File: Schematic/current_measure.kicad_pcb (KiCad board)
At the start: 2 copper layers, 55 x 30.5 mm, 56 parts, among them J1 Conn_01x04_Pin, J2 Conn_01x02, J3 Screw_Terminal_01x02, J4 PowerSupply select, J5 Conn_02x03_Counter_Clockwise, J6 Conn_01x04, Q1 Si2319CDS, SW1 SW_Push, U1 MIC5365-3.3YD5, U2 INA186, U3 ISO652, U4 MCP6002-xSN, U5 OPA350, U6 STM32G431C8Tx, Y1 8MHz

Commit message: PCB small
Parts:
- removed the C11 at (179.4, 78.4)
- removed C22: 1µ, Capacitor_SMD:C_0805_2012Metric
- removed C23: 0.1µ, Capacitor_SMD:C_0805_2012Metric
- removed the C3 at (213.5, 63.5)
- removed J4: PowerSupply select, Connector_PinSocket_2.54mm:PinSocket_1x03_P2.54mm_Vertical
- added C20: 100n, Capacitor_SMD:C_0805_2012Metric, F.Cu at (103.0, 38.5)
- added JP1: SolderJumper_3_Open, Jumper:SolderJumper-3_P1.3mm_Open_Pad1.0x1.5mm, F.Cu at (77.8, 46.8)
- added U7: OPA333xxDBV, Package_TO_SOT_SMD:SOT-23-5_HandSoldering, F.Cu at (106.8, 39.0)
- RV1, RV2: footprint Potentiometer_THT:Potentiometer_Vishay_T73YP_Vertical -> Potentiometer_THT:Potentiometer_Bourns_3296Z_Horizontal
- U4: value MCP6002-xSN -> OPA333xxDBV; footprint Package_SO:SOIC-8_3.9x4.9mm_P1.27mm -> Package_TO_SOT_SMD:SOT-23-5
- Y1: footprint Crystal:Resonator_SMD-3Pin_7.2x3.0mm -> Crystal:Resonator_SMD_Murata_CSTxExxV-3Pin_3.0x1.1mm
- moved J2 180.9 mm to (83.0, 52.5), turned to 90 degrees
- moved D1 180.1 mm to (82.2, 48.2), turned to -90 degrees
- moved D2 171.4 mm to (77.8, 41.8), turned to -90 degrees
- moved U1 170.2 mm to (85.5, 40.8), turned to 90 degrees
- moved J3 143.8 mm to (79.8, 30.8), turned to -90 degrees
- moved R7 140.7 mm to (96.0, 44.8), turned to 180 degrees
- moved R5 139.3 mm to (95.8, 37.0), turned to 180 degrees
- moved J1 139.2 mm to (127.4, 27.4), turned to -90 degrees
- moved R2 138.4 mm to (84.6, 32.0), turned to -90 degrees
- moved U5 137.0 mm to (95.8, 41.0), turned to 180 degrees
- moved U3 136.6 mm to (121.5, 33.5)
- moved R3 135.9 mm to (87.6, 33.0), turned to 0 degrees
- moved D4 135.7 mm to (128.5, 40.7), turned to -90 degrees
- moved D3 134.3 mm to (128.2, 48.0), turned to 90 degrees
- moved R6 133.8 mm to (94.0, 35.0), turned to 0 degrees
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- renumbered C12 to C10, C13 to C11, C14 to C12, C15 to C13, C16 to C14, C17 to C15, C18 to C16, C19 to C17, C20 to C18, C21 to C19, C4 to C3, C5 to C4, C6 to C5, C7 to C6, C8 to C7, C9 to C8, C10 to C9
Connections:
- net /xTAL_{1} renamed /xTAL+
- net /xTAL_{2} renamed /xTAL-
- J5 pad 6: Net-(J4-Pin_2) -> /V_{prog}
- J6 pad 1: GND -> MCU_I2C_SDA
- J6 pad 3: MCU_I2C_SDA -> +3.3V
- J6 pad 4: +3.3V -> GND
- R4 pad 2: Net-(U4A-+) -> Net-(U4-+)
- R5 pad 1: Net-(U5-+) -> Net-(U5--)
- R6 pad 2: Net-(U5-+) -> Net-(U5--)
- R8 pad 2: Net-(U5--) -> Net-(U5-+)
- R9 pad 1: Net-(U5--) -> Net-(U5-+)
- RV1 pad 1: Net-(U4A-+) -> GND
- RV1 pad 2: GND -> Net-(U4-+)
- RV1 pad 3: GND -> Net-(U4-+)
- RV2 pad 1: Net-(U5--) -> Net-(U5-+)
- U4 pad 2: REF_{offset} -> +3.3V
- U4 pad 3: Net-(U4A-+) -> Net-(U4-+)
- U4 pad 4: GND -> REF_{offset}
- U4 pad 5: V_{ref} -> GND
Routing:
- net /V_{prog}: track 0.00 -> 48.0 mm, vias 0 -> 6
- net GND: track 1.50 -> 34.0 mm, vias 7 -> 45
- net +5V: track 0.00 -> 29.1 mm, vias 0 -> 2
- net +3.3V: track 0.00 -> 27.2 mm, vias 0 -> 37
- net /~{RESET}: track 0.00 -> 23.9 mm, vias 0 -> 2
- net +3.3VP: track 0.00 -> 21.7 mm, vias 0 -> 2
- net Net-(U4-+): track 0.00 -> 20.4 mm
- net GPIO_LED: track 0.00 -> 19.7 mm, vias 0 -> 2
- net MCU_I2C_SCL: track 0.00 -> 18.9 mm, vias 0 -> 1
- net V_{buf}: track 0.00 -> 16.3 mm
- net MCU_RxD: track 0.00 -> 15.8 mm
- net MCU_I2C_SDA: track 0.00 -> 15.6 mm, vias 0 -> 1
- net ADC_in: track 0.00 -> 15.1 mm
- net MCU_TxD: track 0.00 -> 14.6 mm
- net Net-(U5-+): track 0.00 -> 14.5 mm, vias 0 -> 1
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- added copper zone on In2.Cu, net +3.3V
- added copper zone on B.Cu, net /V_{prog}
- added copper zone on F.Cu, net /V_{prog}
- added copper zone on In1.Cu, net GND
- removed copper zone on F.Cu, net USB_+5
- removed copper zone on F.Cu, net USB_GND
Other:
- board size 55 x 30.5 mm -> 55 x 30 mm
- copper layers 2 -> 4
- board text added: "3V3"
- board text added: "5V"
- board text added: "Display"
- board text added: "GND"
- board text added: "Reset"
- board text added: "Rx"
- board text added: "SCL"
- board text added: "SDA"
- board text added: "Tx"

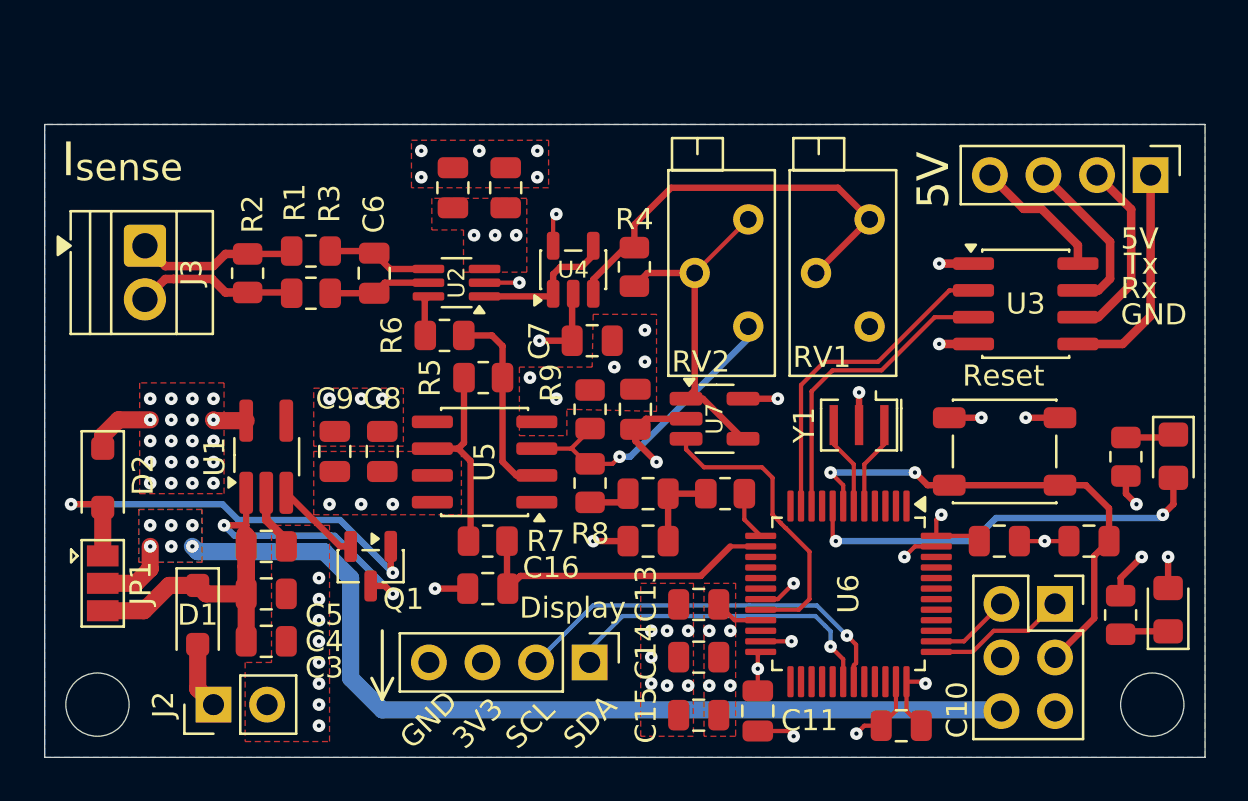
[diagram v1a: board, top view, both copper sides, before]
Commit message: Fix small issues with I2C and add power cap
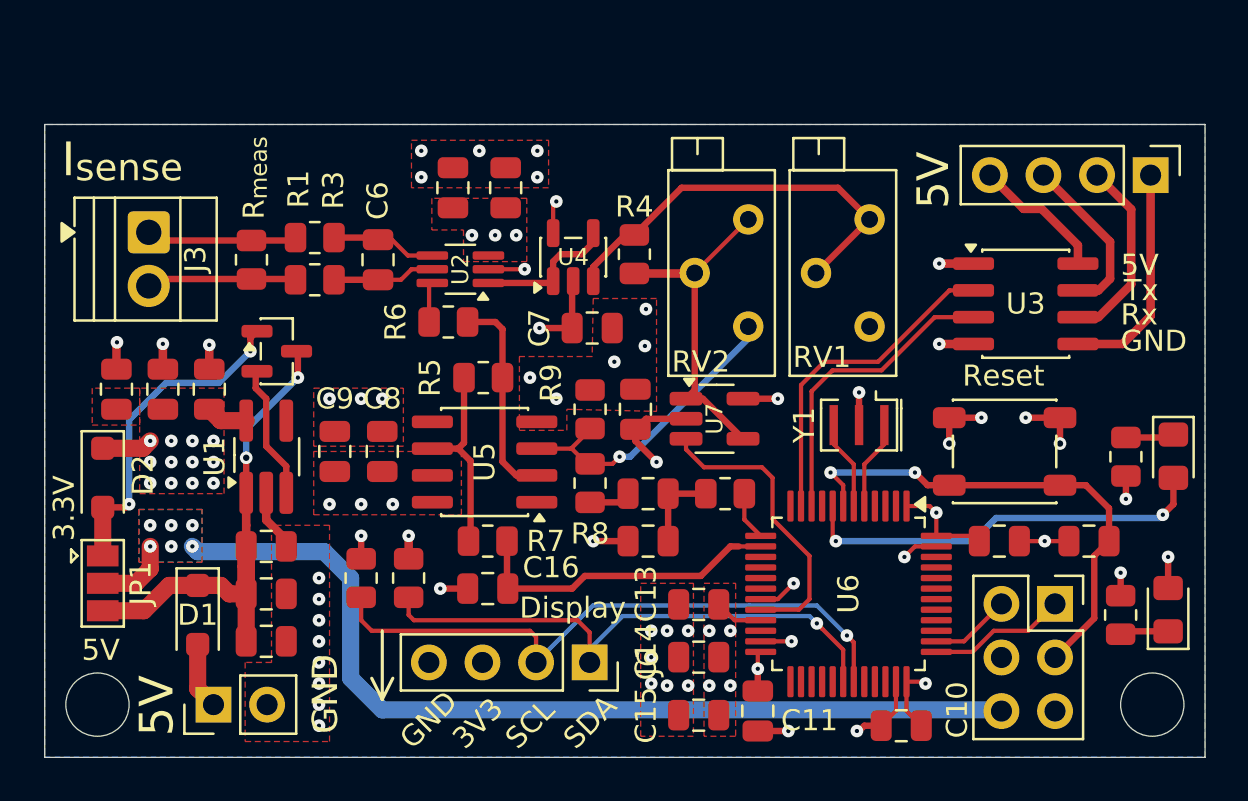
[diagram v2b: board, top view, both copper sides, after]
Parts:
- added C21: 10u, Capacitor_SMD:C_0805_2012Metric, F.Cu at (78.4, 37.5)
- added C22: 1u, Capacitor_SMD:C_0805_2012Metric, F.Cu at (80.6, 37.5)
- added C23: 100n, Capacitor_SMD:C_0805_2012Metric, F.Cu at (82.8, 37.5)
- added R13: 4.7k, Resistor_SMD:R_0805_2012Metric, F.Cu at (90.0, 46.5)
- added R14: 4.7k, Resistor_SMD:R_0805_2012Metric, F.Cu at (92.2, 46.5)
- J6: footprint Connector_PinHeader_2.54mm:PinHeader_1x04_P2.54mm_Vertical -> Connector_PinSocket_2.54mm:PinSocket_1x04_P2.54mm_Vertical
- moved Q1 11.1 mm to (86.0, 35.8), turned to 0 degrees
- moved R6 0.66 mm to (94.1, 34.4)
- moved J3 0.66 mm to (79.9, 30.1)
- moved U2 0.66 mm to (94.7, 31.9)
- moved R3 0.66 mm to (87.8, 32.4)
- moved R1 0.66 mm to (87.8, 30.4)
- moved C6 0.66 mm to (90.8, 31.4)
- moved R2 0.66 mm to (84.8, 31.4)
- moved C7 0.60 mm to (101.0, 34.6)
- moved R4 0.60 mm to (103.0, 31.1)
- moved U4 0.60 mm to (100.0, 31.3)
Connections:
- U6 pad 1: unconnected-(U6-VBAT-Pad1) -> +3.3V
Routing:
- net MCU_I2C_SDA: track 15.6 -> 26.7 mm
- net MCU_I2C_SCL: track 18.9 -> 29.7 mm
- net +3.3VP: track 21.7 -> 15.8 mm
- net +5V: track 29.1 -> 24.5 mm
- net GND: track 34.0 -> 37.9 mm, vias 45 -> 50
- net +3.3V: track 27.2 -> 30.4 mm, vias 37 -> 31
- net Net-(Q1-S): track 4.10 -> 6.39 mm
- net Net-(U4-+): track 20.4 -> 19.1 mm
- net Net-(U5--): track 9.42 -> 9.98 mm
- net /I_{sense}-: track 7.64 -> 7.11 mm
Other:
- board text added: "3.3V"
- board text added: "R_{meas}"
- board text added: "Small current measure"
- board text added: "Łukasz Przystupa"
